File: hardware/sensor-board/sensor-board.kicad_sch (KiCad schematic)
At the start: 55 parts, among them J1 HELM, J2 TACH, J3 PROBES, J4 RPi GPIO, U1 ADS1115IDGSR, U2 ADS1115IDGSR, U3 PC817

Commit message: Sensor board rev 1.1: isolated NMEA 2000 on the board
The Fusion stereo (and the depth transducer) now reach the Pi through the
sensor board itself, not a separate CAN HAT:

- MCP2518FD CAN FD controller on SPI0 (GPIO 8-11), interrupt on GPIO 25,
  40 MHz oscillator: Raspberry Pi OS's mcp251xfd overlay makes it can0
- ISO1044 isolated transceiver; the network side is powered from NET-S
  through reverse-polarity, surge and ESD protection and a 5 V regulator,
  referenced to the network's own ground (about 1 LEN)
- J5, a 5-pin locking plug for a drop cable, Micro-C pin order; a 120 ohm
  bench-only terminator behind an open solder jumper
- the network side is its own island: 2 mm from all other copper (DRC rule),
  its own ground pour, kept clear of the Pi mounting hole beside it

The board grows from 65 x 56 to 65 x 76 mm on the side away from the header
(the tach moves down with it, both field plugs on the bottom edge), with a
fifth mounting hole. ERC, DRC and schematic parity all clean.

Also fixes the schematic generator: two symbols derived from one library
parent (SMAJ5.0A, SMAJ18A) shared their unit lists, so renaming one renamed
both and KiCad refused the file; and custom-shaped pads (SOT-89 tab, solder
jumper) are now routed around by their true outline.

Co-Authored-By: Claude Opus 5.5 <noreply@anthropic.com>
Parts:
- added C12, C14, C15, C18: 100n, sensor-board:C_0805_2012Metric_NoSilk, symbol Device:C
- added C13, C17: 1u, sensor-board:C_0805_2012Metric_NoSilk, symbol Device:C
- added C16: 1u, sensor-board:C_1206_3216Metric_NoSilk, symbol Device:C
- added D10: SMAJ18A, Diode_SMD:D_SMA, symbol Diode:SMAJ18A
- added D11: NUP2105L, sensor-board:SOT-23_NoSilk, symbol Power_Protection:NUP2105L
- added D9: SS14, Diode_SMD:D_SMA, symbol Diode:SS14
- added H5: MountingHole, MountingHole:MountingHole_2.7mm_M2.5, symbol Mechanical:MountingHole
- added J5: NMEA 2000, Connector_Phoenix_MC:PhoenixContact_MC_1,5_5-GF-3.81_1x05_P3.81mm_Horizontal_ThreadedFlange, symbol Connector_Generic:Conn_01x05
- added JP1: TERM, Jumper:SolderJumper-2_P1.3mm_Open_RoundedPad1.0x1.5mm, symbol Jumper:SolderJumper_2_Open
- added R26: 120, sensor-board:R_0805_2012Metric_NoSilk, symbol Device:R
- added R27, R28: 10k, sensor-board:R_0805_2012Metric_NoSilk, symbol Device:R
- added U4: MCP2518FD, Package_SO:SOIC-14_3.9x8.7mm_P1.27mm, symbol Interface_CAN_LIN:MCP2517FD-xSL
- added U5: ISO1044BD, Package_SO:SOIC-8_3.9x4.9mm_P1.27mm, symbol Interface_CAN_LIN:ISO1044BD
- added U6: L78L05, Package_TO_SOT_SMD:SOT-89-3, symbol Regulator_Linear:L78L05_SOT89
- added Y1: 40MHz, Oscillator:Oscillator_SMD_Abracon_ASE-4Pin_3.2x2.5mm, symbol Oscillator:ASE-xxxMHz
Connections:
- net +3V3: now also C12.1, C13.1, C14.1, C15.1, R27.2, R28.2, U4.14 (VDD), U5.1 (VCC1), Y1.1 (EN), Y1.4 (Vdd)
- net GND: now also C12.2, C13.2, C14.2, C15.2, U4.7 (VSS), U5.4 (GND1), Y1.2 (GND)
- net SPI_MOSI: now reaches J4.19 (Pin_19)
- net SPI_MOSI: now also U4.11 (SDI)
- net SPI_MISO: now reaches J4.21 (Pin_21)
- net SPI_MISO: now also U4.12 (SDO)
- net CAN_INT: now reaches J4.22 (Pin_22)
- net CAN_INT: now also R28.1, U4.4 (~{INT})
- net SPI_SCLK: now reaches J4.23 (Pin_23)
- net SPI_SCLK: now also U4.10 (SCK)
- net SPI_CE0: now reaches J4.24 (Pin_24)
- net SPI_CE0: now also R27.1, U4.13 (~{CS})
- new net CAN_CLK: U4.6 (OSC1), Y1.3 (OUT)
- new net CAN_RXD: U4.2 (RXCAN), U5.3 (RXD)
- new net CAN_TXD: U4.1 (TXCAN), U5.2 (TXD)
- new net N2K_12V: C16.1, D10.1 (A1), D9.1 (K), U6.3 (IN)
- new net N2K_5V: C17.1, C18.1, U5.8 (VCC2), U6.1 (OUT)
- new net N2K_GND: C16.2, C17.2, C18.2, D10.2 (A2), D11.3 (A), J5.3 (Pin_3), U5.7 (GND2), U6.2 (GND)
- new net N2K_H: D11.1 (K), J5.4 (Pin_4), R26.1, U5.6 (CANH)
- new net N2K_L: D11.2 (K), J5.5 (Pin_5), JP1.2 (B), U5.5 (CANL)
- new net N2K_NET_S: D9.2 (A), J5.2 (Pin_2)
- new net N2K_TERM: JP1.1 (A), R26.2
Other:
- note added: "NMEA 2000 (Fusion stereo, depth transducer): J5 takes a drop cable -- 1 shield (not connected), 2 NET-S, 3 NET-C, 4 NET-H, 5 NET-L. U5 isolates the network from the Pi: its network side runs from NET-S through D9 (reverse polarity), D10 (surges) and U6 (5 V), and N2K_GND is the network's 0 V, not the Pi's GND. Keep every N2K_* net 2 mm from all other copper (sensor-board.kicad_dru). About 1 LEN. 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"
- note added: "NMEA 2000: Pi side"
- note added: "NMEA 2000: network side (isolated, powered by NET-S)"

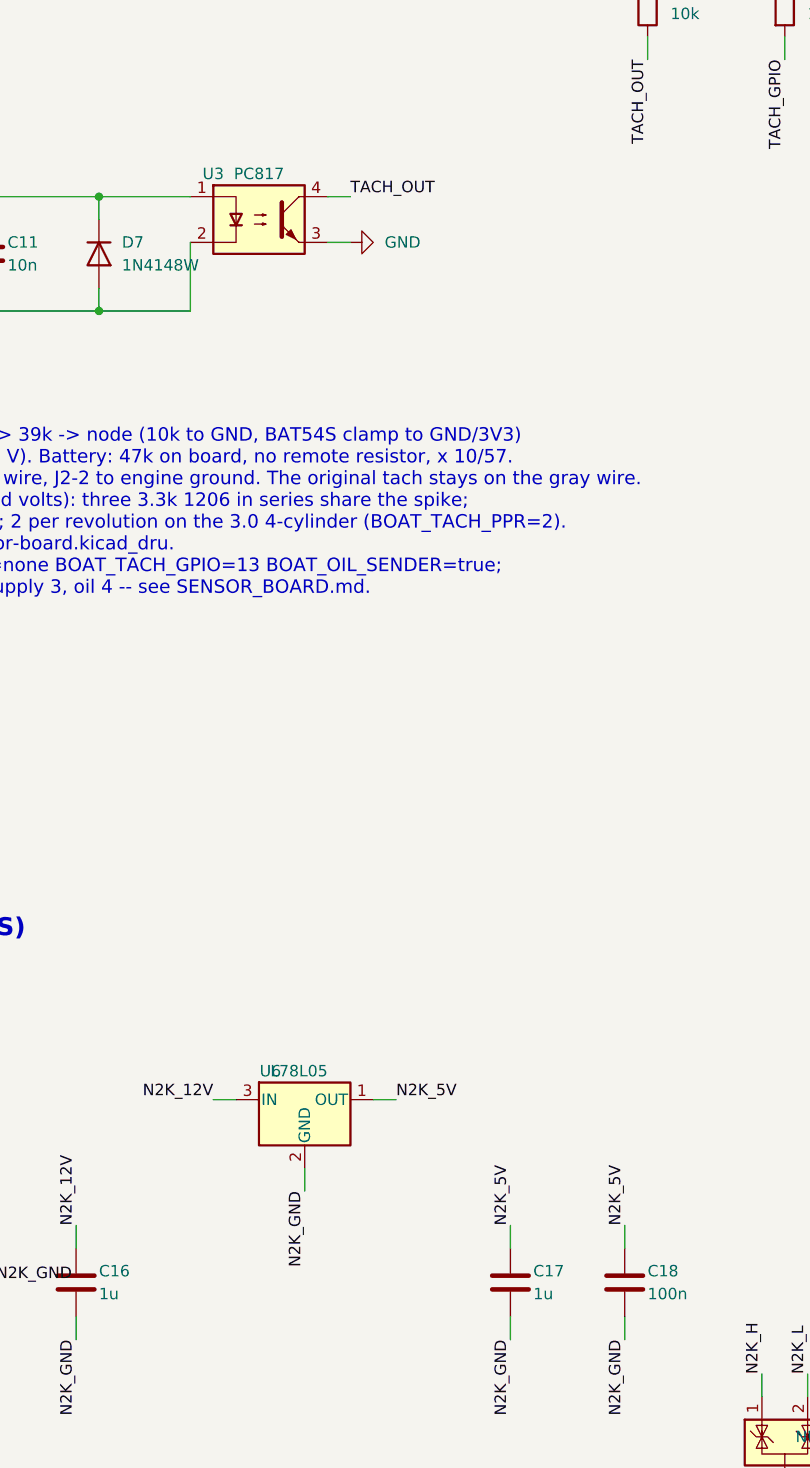
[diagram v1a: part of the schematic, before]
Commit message: Sensor board: pre-order review and PCBWay order package
Checked against the manufacturers' datasheets rather than KiCad's library:
ISO1044 (TI), MCP2518FD (Microchip Table 1-1), uA78L05 SOT-89 (TI),
NUP2105L (onsemi), EL817 incl. its SMD land pattern (Everlight), Abracon ASE.

Changes from the review:
- U6 is now TI's UA78L05ACPK, whose SOT-89 pinout (1 out, 2 gnd, 3 in) was
  read from TI's datasheet; ST's could not be retrieved to confirm
- C17 1 uF -> 4.7 uF: TI asks for ~4.7 uF bulk at the ISO1044's VCC2
- orderable part numbers for U3 (EL817S1(C)(TU)-F), Y1
  (ASE-40.000MHZ-L-C-T) and every Phoenix header and plug
- vias 0.6 -> 0.7 mm (0.2 mm ring; 0.15 was exactly PCBWay's minimum)
- silkscreen stroke 0.12 -> 0.15 mm (PCBWay's minimum)
- PCBWay's limits written into the design rules so DRC enforces them

fab/pcbway/: Gerbers, BOM and centroid in PCBWay's assembly format, and
ORDER.md with every option for the PCB and assembly quote forms.

Co-Authored-By: Claude Opus 5.5 <noreply@anthropic.com>
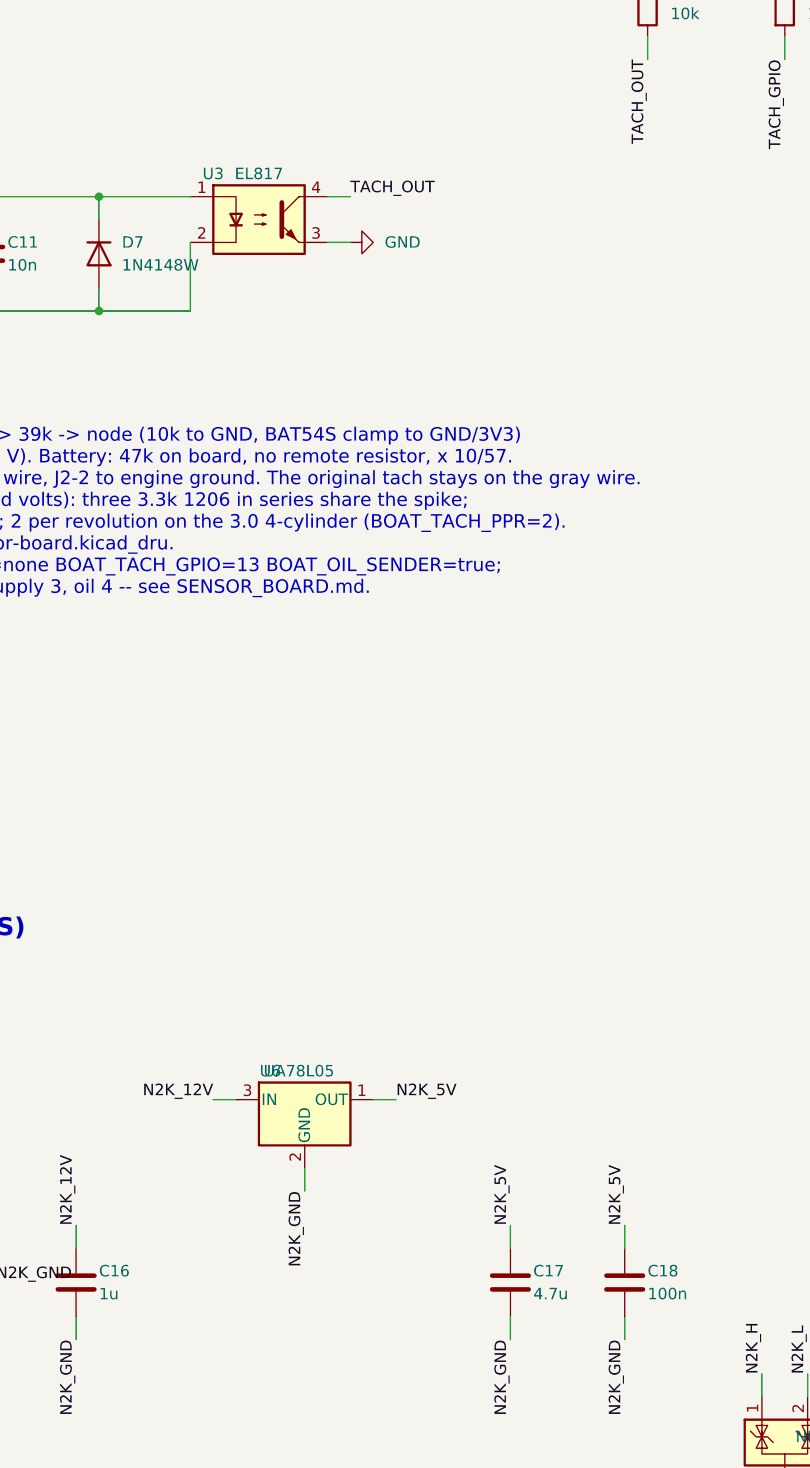
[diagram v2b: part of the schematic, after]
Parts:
- C17: value 1u -> 4.7u; MPN CL21B105KAFNNNE -> CL21A475KAQNNNE; Note regulator output -> regulator output; U5's VCC2 bulk (TI: ~4.7 uF)
- J1: MPN Phoenix MC 1,5/ 8-GF-3,81 (plug: MC 1,5/ 8-STF-3,81) -> Phoenix Contact 1827923 (MC 1,5/ 8-GF-3,81); plug 1827761 (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
- J2: MPN Phoenix MC 1,5/ 2-GF-3,81 (plug: MC 1,5/ 2-STF-3,81) -> Phoenix Contact 1827868 (MC 1,5/ 2-GF-3,81); plug 1827703 (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
- J3: MPN Phoenix MC 1,5/ 3-GF-3,81 (plug: MC 1,5/ 3-STF-3,81) -> Phoenix Contact 1827871 (MC 1,5/ 3-GF-3,81); plug 1827716 (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
- J5: MPN Phoenix MC 1,5/ 5-GF-3,81 (plug: MC 1,5/ 5-STF-3,81) -> Phoenix Contact 1827897 (MC 1,5/ 5-GF-3,81); plug 1827732 (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
- U3: value PC817 -> EL817; MPN PC817 SMD (gull-wing), CTR rank B or C -> EL817S1(C)(TU)-F
- U6: value L78L05 -> UA78L05; MPN L78L05ABUTR -> UA78L05ACPK
- Y1: MPN 40 MHz 3.3 V CMOS oscillator, 3.2 x 2.5 mm (Abracon ASE ser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 -> ASE-40.000MHZ-L-C-T

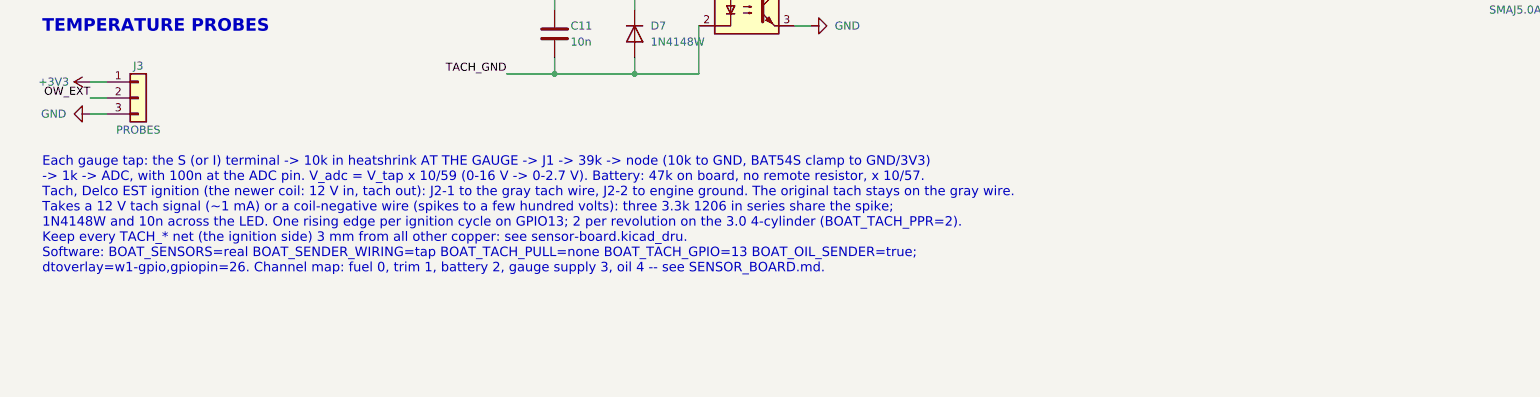
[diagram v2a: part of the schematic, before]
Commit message: Sensor board rev 1.2: every connector pin labelled on the board
Each pin of J1, J2, J3 and J5 now has its connection printed beside it, on
the wire side of the connector: FUEL TRIM BAT+ IGN OIL SPARE GND GND on the
helm connector, TACH/GND on the tach, 3V3/DATA/GND on the probes, and the
NMEA 2000 drop cable's wire colours on J5. The numbered pinout block in the
middle is replaced by a WIRING block that says where each kind of wire goes.

Tach wording is for the newer EST coil only (BAT in, TACH out). The input
itself is unchanged: the coil's TACH terminal is its switched side and
spikes to a few hundred volts, which is what the optocoupler input is for.

Parts moved to make room for the labels; the pour is filled after the
board's connectivity is rebuilt, so slivers between the NMEA 2000 pads are
removed instead of left as floating copper. ERC, DRC and parity: clean.

Co-Authored-By: Claude Opus 5.5 <noreply@anthropic.com>
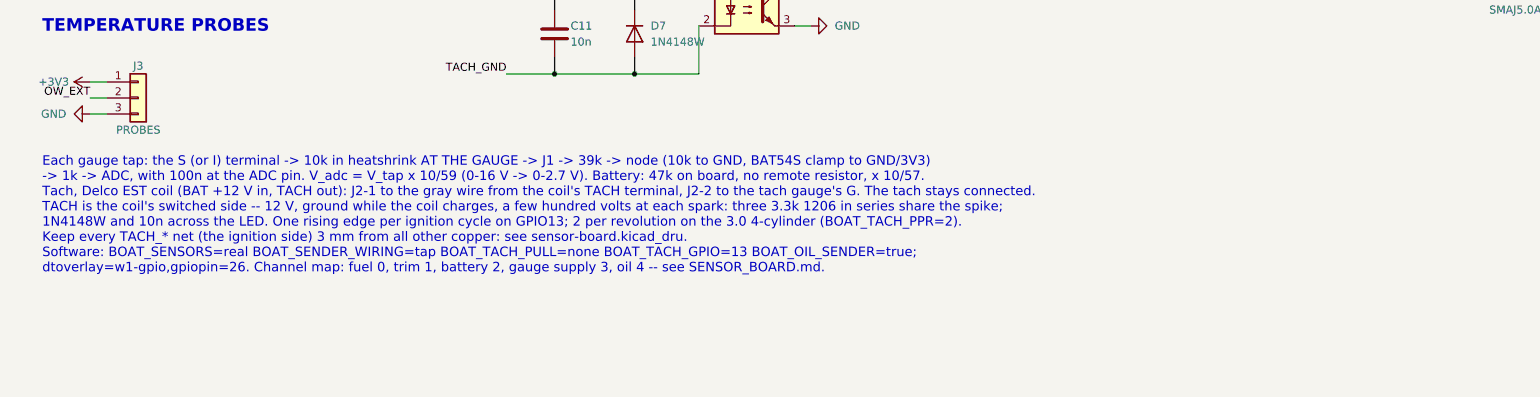
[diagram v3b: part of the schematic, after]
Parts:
- J1: Note 1 fuel S, 2 trim S, 3 battery +12V, 4 gauge I, 5 oil S, 6 s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 -> FUEL/TRIM/OIL: that gauge's S terminal; BAT+: +12V always o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
- J2: Note Delco EST: 1 gray tach wire, 2 engine ground -> TACH: the gray wire (EST coil TACH terminal); GND: the tach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
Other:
- note added: "Each gauge tap: the S (or I) terminal -> 10k in heatshrink AT THE GAUGE -> J1 -> 39k -> node (10k to GND, BAT54S clamp to GND/3V3) -> 1k -> ADC, with 100n at the ADC pin. V_adc = V_tap x 10/59 (0-16 V -> 0-2.7 V). Battery: 47k on board, no remote resistor, x 10/57. Tach, Delco EST coil (BAT +12 V in, TACH out): J2-1 to the gray wire from the coil's TACH terminal, J2-2 to the tach gauge's G. The t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"
- note removed: "Each gauge tap: the S (or I) terminal -> 10k in heatshrink AT THE GAUGE -> J1 -> 39k -> node (10k to GND, BAT54S clamp to GND/3V3) -> 1k -> ADC, with 100n at the ADC pin. V_adc = V_tap x 10/59 (0-16 V -> 0-2.7 V). Battery: 47k on board, no remote resistor, x 10/57. Tach, Delco EST ignition (the newer coil: 12 V in, tach out): J2-1 to the gray tach wire, J2-2 to engine ground. The original tach st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"

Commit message: Sensor board: J6 LIGHTS connector for a separate LED board
The LED controllers stay off this board (strip current next to the gauge
taps, and a shorted strip taking the engine data down with it). J6 gives
a future LED board what it needs from the Pi and nothing it switches:
3V3 for its logic, the I2C bus for PCA9685 PWM channels (as many as
needed), GPIO18 and GPIO19 (PWM0/PWM1) for two addressable strips, GPIO21
spare, and two grounds. JST GH 8-way, latching, SMD on the right edge
between the probe connector and the mounting hole; pins labelled on the
silkscreen.

The two lines from the header's far corner route on the bottom layer so
they don't wall off the header's GND pin 39 from the top pour. J6's GND
vias go in before routing. BOM marks J6 SMD (only the Phoenix blocks and
the header are through-hole). SENSOR_BOARD.md documents the interface and
the rules for the LED board; README points to it.

ERC, DRC and parity: clean.

Co-Authored-By: Claude Opus 5.5 <noreply@anthropic.com>
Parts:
- added J6: LIGHTS, Connector_JST:JST_GH_SM08B-GHS-TB_1x08-1MP_P1.25mm_Horizontal, symbol Connector_Generic:Conn_01x08
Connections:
- net +3V3: now also J6.1 (Pin_1)
- net GND: now also J6.4 (Pin_4), J6.7 (Pin_7)
- net SCL: now also J6.3 (Pin_3)
- net SDA: now also J6.2 (Pin_2)
- net LIGHT_DAT1: now reaches J4.12 (Pin_12)
- net LIGHT_DAT1: now also J6.5 (Pin_5)
- net LIGHT_DAT2: now reaches J4.35 (Pin_35)
- net LIGHT_DAT2: now also J6.6 (Pin_6)
- net LIGHT_AUX: now reaches J4.40 (Pin_40)
- net LIGHT_AUX: now also J6.8 (Pin_8)
- no-connect marks 30 -> 27
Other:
- note added: "J6 carries logic only: the strips' 12 V and current stay on the LED board. PWM strips: PCA9685s on SDA/SCL (not 0x48/0x49, the converters, or 0x70). Addressable strips: DAT1 = GPIO18 (PWM0), DAT2 = GPIO19 (PWM1), 3.3 V: buffer to 5 V there. AUX = GPIO21, spare. 3V3 for the LED board's logic, under 50 mA."
- note added: "LIGHTS: to a separate LED board"

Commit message: Engine temperature from the temp gauge's own sender (J1.6 is now TEMP)
The boat has a temperature gauge with a sender on the engine, so the
board's spare tap becomes TEMP (same circuit; label, net names, docs).

Software (BOAT_TEMP_SENDER=true): the sender is a thermistor, and its
absolute resistance -- which differs between makes, and halves on a
dual-station sender -- folds into the divider fit as the fuel sender's
does. Only the curve's shape matters, and the published curves agree on
it (B about 3900-4000 K). So a cold point (the air or lake temperature
after the engine has sat) and a warm point calibrate the whole gauge,
overheat included: straight lines through the same two points read an
overheat 15-45 F low in simulation; this reads within 5 F even for a
sender at B 3700 K. Three or more widely spread points the published B
can't fit choose their own; points no B fits fall back to straight lines
and say so. A tap wire off is no reading, not boiling.

Coolant source order: a NMEA 2000 converter, then the gauge's sender,
then a clamp-on DS18B20, which fills in with the key off. The probe
offset is refused while the gauge is the source. New Engine temperature
card on /calibrate.

540 tests pass. ERC, DRC and parity: clean.

Co-Authored-By: Claude Opus 5.5 <noreply@anthropic.com>
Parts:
- J1: Note FUEL/TRIM/OIL: that gauge's S terminal; BAT+: +12V always o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 -> FUEL/TRIM/OIL/TEMP: that gauge's S terminal; BAT+: +12V alw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
- U2: Note I2C 0x49: oil, spare (optional) -> I2C 0x49: oil, engine temperature
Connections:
- net SPARE_ADC renamed TEMP_ADC
- net SPARE_DIV renamed TEMP_DIV
- net SPARE_IN renamed TEMP_IN
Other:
- note added: "TEMP: J1.6 -> U2 AIN1"
- note removed: "SPARE: J1.6 -> U2 AIN1"

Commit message: Sensor board: 5 V input (J7) that powers the Pi through the header
The Pi now runs from an external 12 V -> 5 V converter wired to J7 on the
board, through the header's 5 V pins (back-powering, 5 V +/-5 %, up to
2.5 A per the HAT guide); the board's 3V3 comes from the Pi as before.

An ideal diode sits in the way (TI LM74700-Q1 driving an IRLML0030): about
20 mV drop where a Schottky's 0.4 V would trip the Pi's undervoltage
warning. J7 wired backwards is blocked, and the Pi's USB-C can't push
current back into the converter. SMAJ5.0A clamp and 22 uF bulk on the
rail. Not protected: a converter failing with 12 V out (docs say to buy
one with output OVP).

The Pi's 5 V pins are in the header's top-left corner, boxed in by J1 and
a mounting hole, so J7 and the ideal diode go on a 35 x 12 mm tab above
the left half of the header (board now 65 x 88 overall). The router takes
an origin and off-board notches for that. Also:
- the 5 V current path routes wide first, sense pins and caps thin after;
  its run to the header goes on the bottom layer, where on top it walled
  off the header's GND pin 6 from the pour;
- vias keep their drill 0.25 mm off their own net's SMD pads (the router
  had put one on Q1's drain pad); none on the board now;
- BAT+ is documented as the dashboard switch's 12 V, the converter's feed.

ERC, DRC and parity: clean.

Co-Authored-By: Claude Opus 5.5 <noreply@anthropic.com>
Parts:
- added C19, C20: 100n, sensor-board:C_0805_2012Metric_NoSilk, symbol Device:C
- added C21: 22u, sensor-board:C_1206_3216Metric_NoSilk, symbol Device:C
- added D12: SMAJ5.0A, Diode_SMD:D_SMA, symbol Diode:SMAJ5.0A
- added J7: 5V IN, Connector_Phoenix_MC:PhoenixContact_MC_1,5_2-GF-3.81_1x02_P3.81mm_Horizontal_ThreadedFlange, symbol Connector_Generic:Conn_01x02
- added Q1: IRLML0030, Package_TO_SOT_SMD:SOT-23, symbol Transistor_FET:IRLML0030
- added U7: LM74700-Q1, Package_TO_SOT_SMD:SOT-23-6, symbol Power_Management:LM74700
- J1: Note FUEL/TRIM/OIL/TEMP: that gauge's S terminal; BAT+: +12V alw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 -> FUEL/TRIM/OIL/TEMP: that gauge's S terminal; BAT+: the dash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
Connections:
- net GND: now also C20.2, C21.2, D12.2 (A2), J7.2 (Pin_2), U7.2 (GND)
- net +5V: now reaches J4.2 (Pin_2)
- net +5V: now also J4.4 (Pin_4), C21.1, D12.1 (A1), Q1.3 (D), U7.4 (CATHODE)
- new net IDEAL_G: Q1.1 (G), U7.5 (GATE)
- new net VCAP: C19.1, U7.1 (VCAP)
- new net VIN: C19.2, C20.1, J7.1 (Pin_1), Q1.2 (S), U7.3 (EN), U7.6 (ANODE)
- no-connect marks 27 -> 25
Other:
- note added: "5 V IN: from the 12 V -> 5 V converter, to the Pi's 5 V pins"
- note added: "J7 takes the converter's 5 V (set 5.1-5.2 V) and runs the Pi through header pins 2 and 4; this board's 3V3 comes from the Pi. U7 + Q1 are an ideal diode (~20 mV): J7 wired backwards is blocked, and the Pi's USB-C can't feed back into the converter. D12 clamps spikes. A converter failing with 12 V out is not caught here: use one with output overvoltage protection."
